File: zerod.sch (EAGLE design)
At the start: 36 parts, among them IC1 NE5532N, IC2 LM3914N, Q1 2N3906

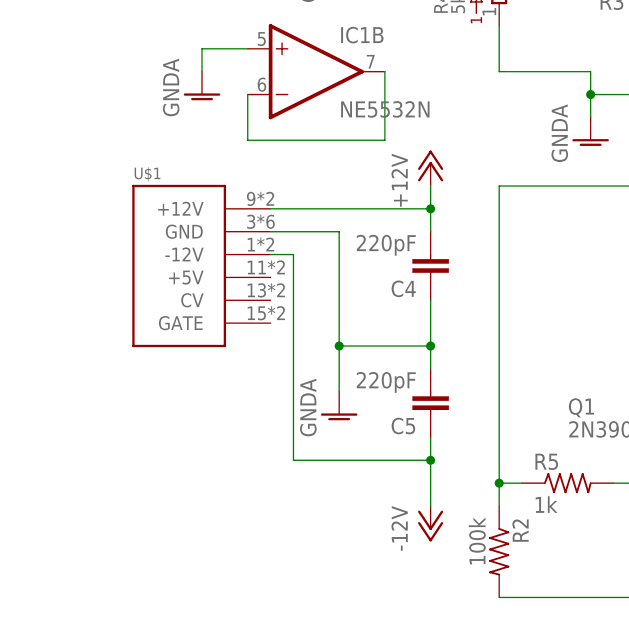
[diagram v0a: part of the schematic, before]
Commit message: routed board to match updated schematic
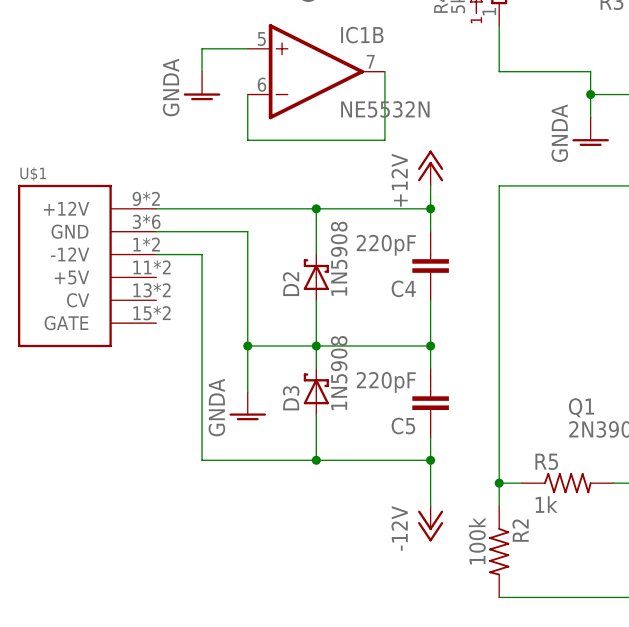
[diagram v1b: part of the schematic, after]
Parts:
- added D2, D3: 1N5908, diode:1N5908
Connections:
- net +12V: now also D2.C
- net -12V: now also D3.A
- net GNDA: now also D2.A, D3.C
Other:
- moved on the sheet: U$1
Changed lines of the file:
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@@
 <grid distance="0.1" unitdist="inch" unit="inch" style="lines" multiple="1" display="no" altdistance="0.01" altunitdist="inch" altunit="inch"/>
 <layers>
-<layer number="1" name="Top" color="4" fill="1" visible="no" active="no"/>
-<layer number="16" name="Bottom" color="1" fill="1" visible="no" active="no"/>
-<layer number="17" name="Pads" color="2" fill="1" visible="no" active="no"/>
-<layer number="18" name="Vias" color="2" fill="1" visible="no" active="no"/>
-<layer number="19" name="Unrouted" color="6" fill="1" visible="no" active="no"/>
-<layer number="20" name="Dimension" color="15" fill="1" visible="no" active="no"/>
-<layer number="21" name="tPlace" color="7" fill="1" visible="no" active="no"/>
-<layer number="22" name="bPlace" color="7" fill="1" visible="no" active="no"/>
-<layer number="23" name="tOrigins" color="15" fill="1" visible="no" active="no"/>
-<layer number="24" name="bOrigins" color="15" fill="1" visible="no" active="no"/>
-<layer number="25" name="tNames" color="7" fill="1" visible="no" active="no"/>
-<layer number="26" name="bNames" color="7" fill="1" visible="no" active="no"/>
-<layer number="27" name="tValues" color="7" fill="1" visible="no" active="no"/>
-<layer number="28" name="bValues" color="7" fill="1" visible="no" active="no"/>
+<layer number="1" name="Top" color="4" fill="1" visible="yes" active="no"/>
+<layer number="16" name="Bottom" color="1" fill="1" visible="yes" active="no"/>
+<layer number="17" name="Pads" color="2" fill="1" visible="yes" active="no"/>
+<layer number="18" name="Vias" color="2" fill="1" visible="yes" active="no"/>
+<layer number="19" name="Unrouted" color="6" fill="1" visible="yes" active="no"/>
+<layer number="20" name="Dimension" color="15" fill="1" visible="yes" active="no"/>
+<layer number="21" name="tPlace" color="7" fill="1" visible="yes" active="no"/>
+<layer number="22" name="bPlace" color="7" fill="1" visible="yes" active="no"/>
+<layer number="23" name="tOrigins" color="15" fill="1" visible="yes" active="no"/>
+<layer number="24" name="bOrigins" color="15" fill="1" visible="yes" active="no"/>
+<layer number="25" name="tNames" color="7" fill="1" visible="yes" active="no"/>
+<layer number="26" name="bNames" color="7" fill="1" visible="yes" active="no"/>
+<layer number="27" name="tValues" color="7" fill="1" visible="yes" active="no"/>
+<layer number="28" name="bValues" color="7" fill="1" visible="yes" active="no"/>
 <layer number="29" name="tStop" color="7" fill="3" visible="no" active="no"/>
 <layer number="30" name="bStop" color="7" fill="6" visible="no" active="no"/>
@@
 <layer number="35" name="tGlue" color="7" fill="4" visible="no" active="no"/>
 <layer number="36" name="bGlue" color="7" fill="5" visible="no" active="no"/>
-<layer number="37" name="tTest" color="7" fill="1" visible="no" active="no"/>
-<layer number="38" name="bTest" color="7" fill="1" visible="no" active="no"/>
+<layer number="37" name="tTest" color="7" fill="1" visible="yes" active="no"/>
+<layer number="38" name="bTest" color="7" fill="1" visible="yes" active="no"/>
 <layer number="39" name="tKeepout" color="4" fill="11" visible="no" active="no"/>
 <layer number="40" name="bKeepout" color="1" fill="11" visible="no" active="no"/>
@@
 <layer number="44" name="Drills" color="7" fill="1" visible="no" active="no"/>
 <layer number="45" name="Holes" color="7" fill="1" visible="no" active="no"/>
-<layer number="46" name="Milling" color="3" fill="1" visible="no" active="no"/>
-<layer number="47" name="Measures" color="7" fill="1" visible="no" active="no"/>
-<layer number="48" name="Document" color="7" fill="1" visible="no" active="no"/>
-<layer number="49" name="Reference" color="7" fill="1" visible="no" active="no"/>
-<layer number="50" name="dxf" color="7" fill="1" visible="no" active="no"/>
-<layer number="51" name="tDocu" color="6" fill="1" visible="no" active="no"/>
-<layer number="52" name="bDocu" color="7" fill="1" visible="no" active="no"/>
-<layer number="53" name="tGND_GNDA" color="7" fill="9" visible="no" active="no"/>
-<layer number="54" name="bGND_GNDA" color="1" fill="9" visible="no" active="no"/>
-<layer number="56" name="wert" color="7" fill="1" visible="no" active="no"/>
+<layer number="46" name="Milling" color="3" fill="1" visible="yes" active="no"/>
+<layer number="47" name="Measures" color="7" fill="1" visible="yes" active="no"/>
+<layer number="48" name="Document" color="7" fill="1" visible="yes" active="no"/>
+<layer number="49" name="Reference" color="7" fill="1" visible="yes" active="no"/>
+<layer number="50" name="dxf" color="7" fill="1" visible="yes" active="no"/>
+<layer number="51" name="tDocu" color="6" fill="1" visible="yes" active="no"/>
+<layer number="52" name="bDocu" color="7" fill="1" visible="yes" active="no"/>
+<layer number="53" name="tGND_GNDA" color="7" fill="9" visible="yes" active="no"/>
+<layer number="54" name="bGND_GNDA" color="1" fill="9" visible="yes" active="no"/>
+<layer number="56" name="wert" color="7" fill="1" visible="yes" active="no"/>
 <layer number="90" name="Modules" color="5" fill="1" visible="yes" active="yes"/>
 <layer number="91" name="Nets" color="2" fill="1" visible="yes" active="yes"/>
@@
 <part name="GND10" library="supply1" deviceset="GNDA" device=""/>
 <part name="PAD4" library="wirepad" deviceset="3,17/1,3" device="" value="output"/>
+<part name="D2" library="diode" deviceset="1N5908" device=""/>
+<part name="D3" library="diode" deviceset="1N5908" device=""/>
 </parts>
 <sheets>
@@
 <instance part="P+3" gate="1" x="160.02" y="76.2"/>
 <instance part="R1" gate="G$1" x="22.86" y="81.28" rot="R180"/>
-<instance part="GND9" gate="1" x="10.16" y="20.32"/>
+<instance part="GND9" gate="1" x="0" y="20.32"/>
 <instance part="P+4" gate="1" x="20.32" y="48.26"/>
 <instance part="P-1" gate="1" x="20.32" y="7.62"/>
-<instance part="U$1" gate="G$1" x="-7.62" y="38.1"/>
+<instance part="U$1" gate="G$1" x="-20.32" y="38.1"/>
 <instance part="C4" gate="G$1" x="20.32" y="35.56" rot="R180"/>
 <instance part="C5" gate="G$1" x="20.32" y="20.32" rot="R180"/>
@@
 <instance part="GND10" gate="1" x="96.52" y="55.88"/>
 <instance part="PAD4" gate="1" x="109.22" y="60.96" rot="R180"/>
+<instance part="D2" gate="1" x="7.62" y="35.56" rot="R90"/>
+<instance part="D3" gate="1" x="7.62" y="22.86" rot="R90"/>
 </instances>
 <busses>
@@
 <segment>
 <pinref part="GND9" gate="1" pin="GNDA"/>
-<wire x1="10.16" y1="22.86" x2="10.16" y2="27.94" width="0.1524" layer="91"/>
+<wire x1="0" y1="22.86" x2="0" y2="27.94" width="0.1524" layer="91"/>
 <wire x1="20.32" y1="33.02" x2="20.32" y2="27.94" width="0.1524" layer="91"/>
 <wire x1="20.32" y1="27.94" x2="20.32" y2="25.4" width="0.1524" layer="91"/>
-<wire x1="10.16" y1="27.94" x2="20.32" y2="27.94" width="0.1524" layer="91"/>
+<wire x1="0" y1="27.94" x2="7.62" y2="27.94" width="0.1524" layer="91"/>
 <junction x="20.32" y="27.94"/>
 <pinref part="C4" gate="G$1" pin="1"/>
 <pinref part="C5" gate="G$1" pin="2"/>
-<wire x1="10.16" y1="27.94" x2="10.16" y2="40.64" width="0.1524" layer="91"/>
-<junction x="10.16" y="27.94"/>
+<wire x1="7.62" y1="27.94" x2="20.32" y2="27.94" width="0.1524" layer="91"/>
+<wire x1="0" y1="27.94" x2="0" y2="40.64" width="0.1524" layer="91"/>
+<junction x="0" y="27.94"/>
 <pinref part="U$1" gate="G$1" pin="GND"/>
-<wire x1="2.54" y1="40.64" x2="10.16" y2="40.64" width="0.1524" layer="91"/>
+<wire x1="-10.16" y1="40.64" x2="0" y2="40.64" width="0.1524" layer="91"/>
+<pinref part="D2" gate="1" pin="A"/>
+<wire x1="7.62" y1="33.02" x2="7.62" y2="27.94" width="0.1524" layer="91"/>
+<junction x="7.62" y="27.94"/>
+<pinref part="D3" gate="1" pin="C"/>
+<wire x1="7.62" y1="25.4" x2="7.62" y2="27.94" width="0.1524" layer="91"/>
 </segment>
 <segment>
@@
 <pinref part="U$1" gate="G$1" pin="+12V"/>
 <wire x1="20.32" y1="43.18" x2="20.32" y2="40.64" width="0.1524" layer="91"/>
-<wire x1="20.32" y1="43.18" x2="2.54" y2="43.18" width="0.1524" layer="91"/>
+<wire x1="20.32" y1="43.18" x2="7.62" y2="43.18" width="0.1524" layer="91"/>
 <junction x="20.32" y="43.18"/>
 <pinref part="C4" gate="G$1" pin="2"/>
+<pinref part="D2" gate="1" pin="C"/>
+<wire x1="7.62" y1="43.18" x2="-10.16" y2="43.18" width="0.1524" layer="91"/>
+<wire x1="7.62" y1="38.1" x2="7.62" y2="43.18" width="0.1524" layer="91"/>
+<junction x="7.62" y="43.18"/>
 </segment>
 </net>
@@
 <pinref part="U$1" gate="G$1" pin="-12V"/>
 <wire x1="20.32" y1="15.24" x2="20.32" y2="17.78" width="0.1524" layer="91"/>
-<wire x1="2.54" y1="38.1" x2="5.08" y2="38.1" width="0.1524" layer="91"/>
-<wire x1="5.08" y1="38.1" x2="5.08" y2="15.24" width="0.1524" layer="91"/>
-<wire x1="5.08" y1="15.24" x2="20.32" y2="15.24" width="0.1524" layer="91"/>
+<wire x1="-10.16" y1="38.1" x2="-5.08" y2="38.1" width="0.1524" layer="91"/>
+<wire x1="-5.08" y1="38.1" x2="-5.08" y2="15.24" width="0.1524" layer="91"/>
+<wire x1="-5.08" y1="15.24" x2="7.62" y2="15.24" width="0.1524" layer="91"/>
 <junction x="20.32" y="15.24"/>
 <pinref part="C5" gate="G$1" pin="1"/>
-</segment>
-</net>
+<pinref part="D3" gate="1" pin="A"/>
+<wire x1="7.62" y1="15.24" x2="20.32" y2="15.24" width="0.1524" layer="91"/>
+<wire x1="7.62" y1="20.32" x2="7.62" y2="15.24" width="0.1524" layer="91"/>
+<junction x="7.62" y="15.24"/>
+</segment>
+</net>
